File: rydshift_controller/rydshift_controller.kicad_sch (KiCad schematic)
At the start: 0 parts

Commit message: Update rydshift_controller PCB design and symbols
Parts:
- added C1, C2: 10n, symbol Device:C
- added C10, C15, C24, C4: 1n, symbol Device:C
- added C11, C12: 4.7n, symbol Device:C
- added C13, C17, C22, C23, C3, C5, C6, C7, C8, C9: 0.1u, symbol Device:C
- added C14, C25: 10u, symbol Device:C
- added C16, C18, C21, C26: 2.2u, symbol Device:C
- added C19, C20: 1.5p, symbol Device:C
- added J1, J2, J3, J4, J5, J6: Conn_Coaxial, symbol Connector:Conn_Coaxial
- added L1, L2, L3, L6: 120n, symbol Device:L
- added L4, L5: 5.1n, symbol Device:L
- added R1, R10, R5, R9: 49.9, symbol Device:R
- added R11, R12: 1.5k, symbol Device:R
- added R2, R3, R7, R8: 100, symbol Device:R
- added R4, R6: 453, symbol Device:R
- added TR1, TR2: ADT9-1T, RF_Mini-Circuits:Mini-Circuits_CD542_H2.84mm, symbol Transformer:ADT9-1T
- added U1, U2: 2 dB atten, RF_Converter:RF_Attenuator_Susumu_PAT1220, symbol RF:PAT1220-C-0DB
- added U10, U11: 10 dB atten, RF_Converter:RF_Attenuator_Susumu_PAT1220, symbol RF:PAT1220-C-0DB
- added U12, U13: ADP-2-1W, RF_Mini-Circuits:Mini-Circuits_CD636_LandPatternPL-035, symbol RF:ADP-2-1W
- added U3: LTC5598IUF-PBF, LTC5598IUF-PBF_ADI, symbol LTC5598:LTC5598IUF-PBF
- added U4, U6: 24 dB atten, RF_Converter:RF_Attenuator_Susumu_PAT1220, symbol RF:PAT1220-C-0DB
- added U5, U7: AD8337BCPZ-REEL, CP_8_13_ADI, symbol AD8337:AD8337BCPZ-REEL
- added U8, U9: TSS-13LN+, DQ1225_MNC, symbol TSS-13LN+:TSS-13LN+
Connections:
- new net: C5.2, L1.2, U5.8 (VPOS)
- new net: C12.1, TR2.3
- new net: C23.1, R12.1
- new net: C26.1, L6.2, R12.2, U9.7 (RF-OUT/DC-IN)
- new net: C18.2, L4.2
- new net: R4.1, U5.1 (VOUT)
- new net: C2.2, U2.1
- new net: R6.1, U7.1 (VOUT)
- new net: C16.1, L3.2, R11.2, U8.7 (RF-OUT/DC-IN)
- new net: C21.1, C23.2, U9.3 (RF-IN)
- new net: C21.2, L5.2
- new net: C7.2, L2.2, U7.8 (VPOS)
- new net: R1.2, U4.2, U5.3 (INPP)
- new net: C11.1, TR1.3
- new net: C11.2, R9.1
- new net: R2.1, R3.2, U5.4 (INPN)
- new net: C17.1, R11.1
- new net: R7.2, R8.1, U7.4 (INPN)
- new net: R8.2, U7.5 (PRAO)
- new net: C1.2, U1.1
- new net: R2.2, U5.5 (PRAO)
- new net: C12.2, R10.1
- new net: C17.2, C18.1, U8.3 (RF-IN)
- new net: R5.2, U6.2, U7.3 (INPP)
- new net +5V: C14.1, C15.2, C24.2, C25.1, C6.2, C9.2, L1.1, L2.1, L3.1, L6.1
- new net -5V: C3.2, C8.2, U5.6 (VNEG), U7.6 (VNEG)
- new net 9959_I_IN: C1.1, J1.1 (In)
- new net 9959_Q_IN: C2.1, J2.1 (In)
- new net GAIN_I: C4.2, J5.1 (In), U5.7 (GAIN)
- new net GAIN_Q: C10.2, J6.1 (In), U7.7 (GAIN)
- new net GND: C10.1, C13.1, C14.2, C15.1, C19.2, C20.2, C22.1, C24.1, C25.2, C3.1, C4.1, C5.1, C6.1, C7.1, C8.1, C9.1, J1.2 (Ext), J2.2 (Ext), J3.2 (Ext), J4.2 (Ext), J5.2 (Ext), J6.2 (Ext), R1.1, R3.1, R5.1, R7.1, TR1.1, TR1.6, TR2.1, TR2.6, U1.3, U10.3, U11.3, U12.6 (GND), U13.6 (GND), U2.3, U4.3, U5.2 (VCOM), U5.9 (EPAD), U6.3, U7.2 (VCOM), U7.9 (EPAD), U8.13 (GND), U9.13 (GND)
- new net I_TSS_in: C19.1, L4.1, TR1.4
- new net I_VGA_out: R4.2, R9.2
- new net I_select: J3.1 (In), U1.2, U4.1
- new net Q_TSS_in: C20.1, L5.1, TR2.4
- new net Q_VGA_out: R10.2, R6.2
- new net Q_select: J4.1 (In), U2.2, U6.1
- new net SHUTDOWN_pre_I: C13.2, U8.1 (VG)
- new net SHUTDOWN_pre_Q: C22.2, U9.1 (VG)
- new net pre1_I_half1: U12.3 (PORT1)
- new net pre1_I_half2: U12.4 (PORT2)
- new net pre1_I_out: C16.2, U10.1
- new net pre1_I_sum: U10.2, U12.1 (SUM)
- new net pre1_Q_half1: U13.3 (PORT1)
- new net pre1_Q_half2: U13.4 (PORT2)
- new net pre1_Q_out: C26.2, U11.1
- new net pre1_Q_sum: U11.2, U13.1 (SUM)
- no-connect marks 0 -> 20
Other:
- added sheet sheet2 (sheet2.kicad_sch)
- note added: "(approx 24-24.5 dB; comp at 22-23 dBm)"
- note added: "(before stage 2)"
- note added: "(to counteract the 24 dB gain of VGA)"
- note added: "Input VGA for I/Q paths"
- note added: "Input and Internal Routing"
- note added: "Matching VGA to predriver"
- note added: "Power Splitters and Conditioning"
- note added: "Stage 1 of Predriver"
- note added: "Z_AD8337 is roughly 500 ohms; -0.46 dB loss from series res"

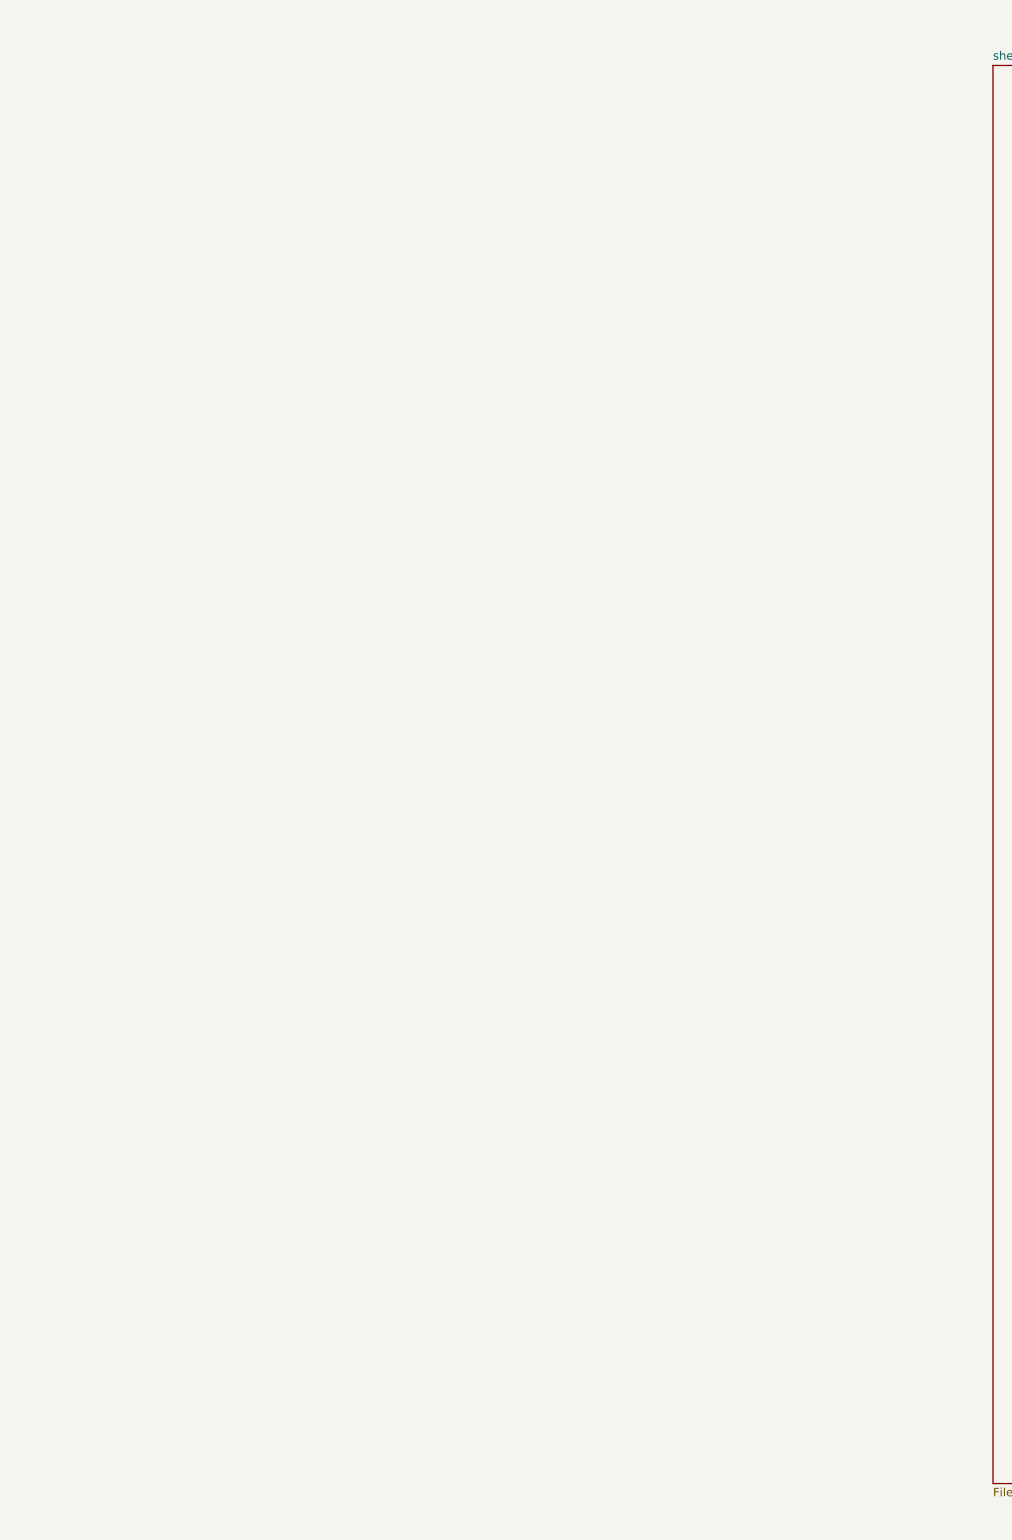
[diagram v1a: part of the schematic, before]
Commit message: bias controller, DAC, and ADCs
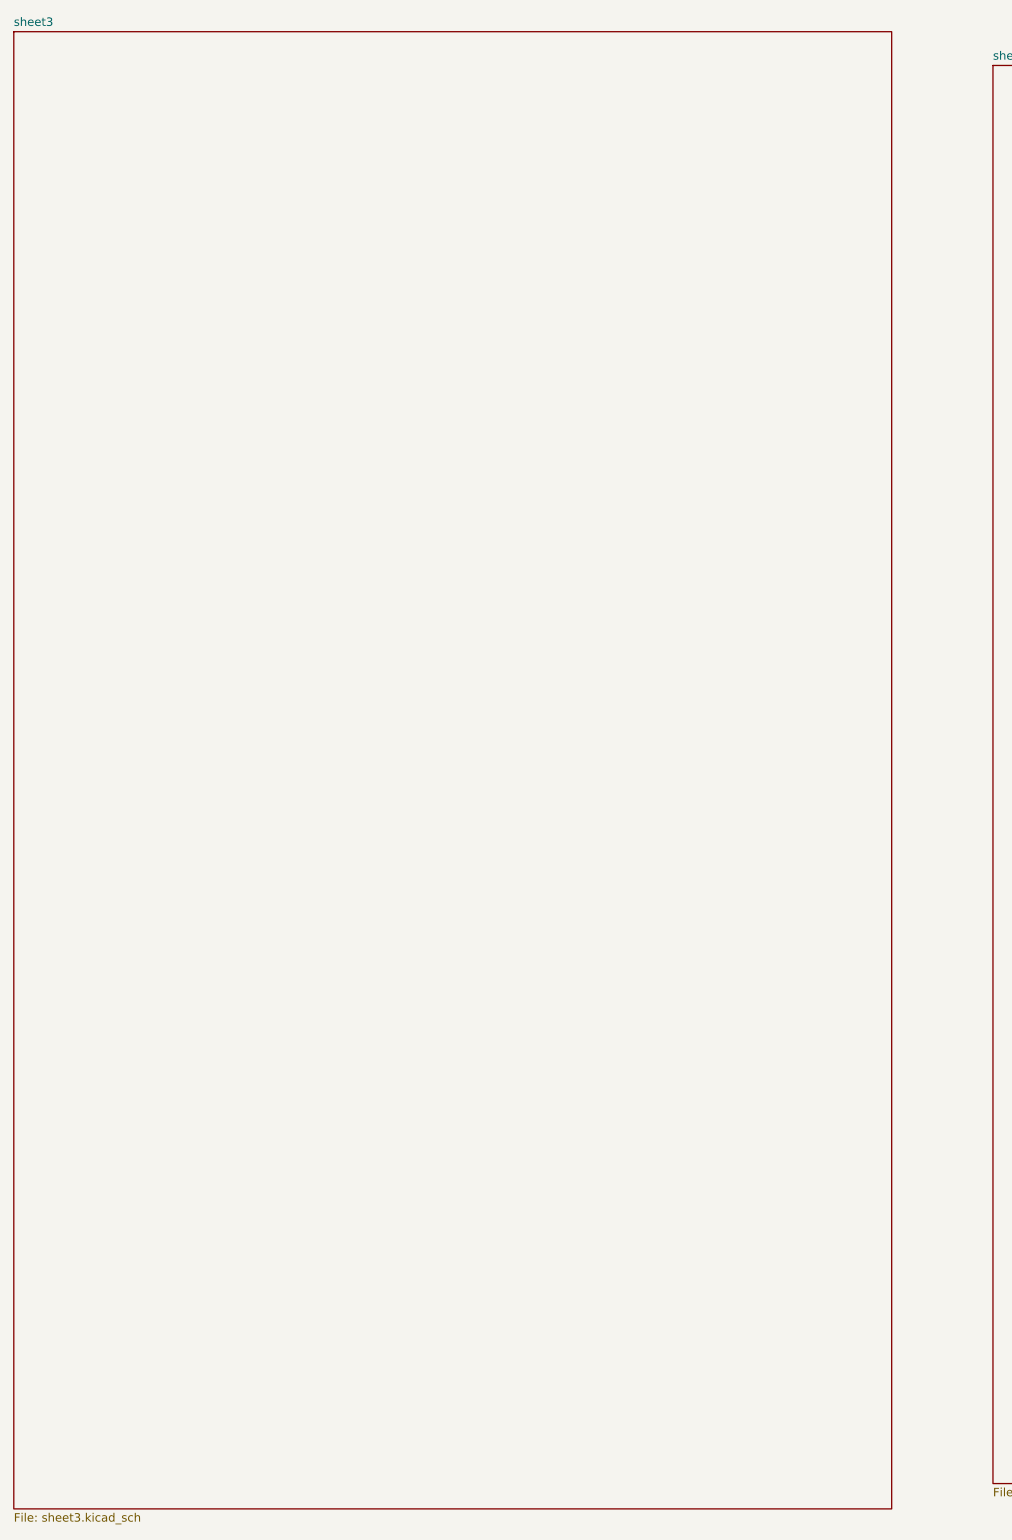
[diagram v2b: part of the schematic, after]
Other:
- added sheet sheet3 (sheet3.kicad_sch)
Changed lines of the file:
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@@
+		)
+	)
+	(sheet
+		(at -347.98 -7.62)
+		(size 132.08 222.25)
+		(exclude_from_sim no)
+		(in_bom yes)
+		(on_board yes)
+		(dnp no)
+		(fields_autoplaced yes)
+		(stroke
+			(width 0.1524)
+			(type solid)
+		)
+		(fill
+			(color 0 0 0 0)
+		)
+		(property "Sheetname" "sheet3"
+			(at -347.98 -8.3316 0)
+			(show_name no)
+			(do_not_autoplace no)
+			(effects
+				(font
+					(size 1.27 1.27)
+				)
+				(justify left bottom)
+			)
+		)
+		(property "Sheetfile" "sheet3.kicad_sch"
+			(at -347.98 215.2146 0)
+			(show_name no)
+			(do_not_autoplace no)
+			(effects
+				(font
+					(size 1.27 1.27)
+				)
+				(justify left top)
+			)
+		)
+		(instances
+			(project "rydshift_controller"
+				(path "/2b15a9df-cbe9-4e34-a5cc-e78006d66b2a"
+					(page "3")
+				)
+			)
 		)
 	)
